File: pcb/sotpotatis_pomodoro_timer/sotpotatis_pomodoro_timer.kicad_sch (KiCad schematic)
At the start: 46 parts, among them J2 USB_C_PWR_IN, SW1 LEFT_BTN, SW2 PRESET_1_BTN, SW3 PRESET_2_BTN, SW4 PRESET_3_BTN, SW5 RIGHT_BTN, SW6 PWR_SWITCH, U1 ATtiny84A-P

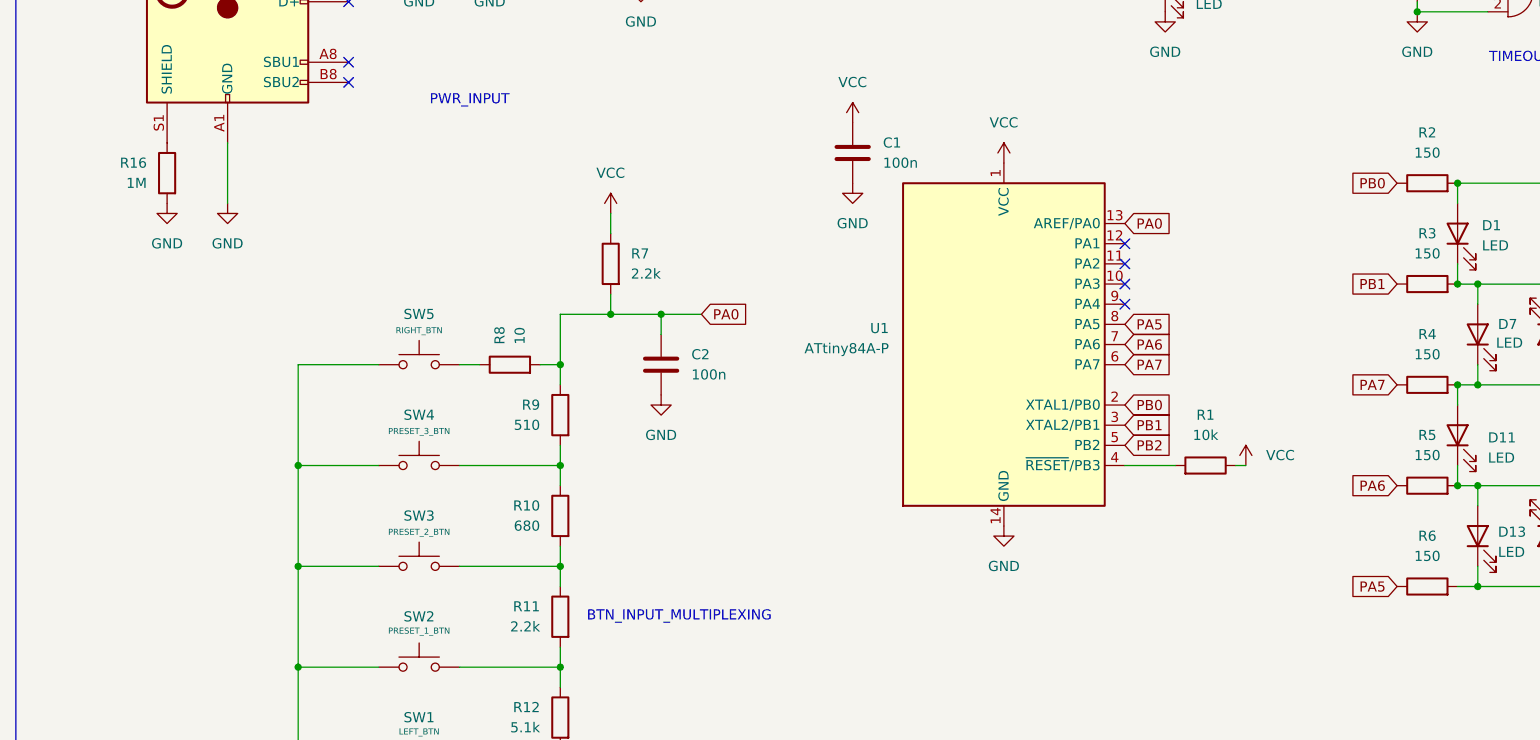
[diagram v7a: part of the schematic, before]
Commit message: fix: Remove 1M shield resistor, component relabels for better layout
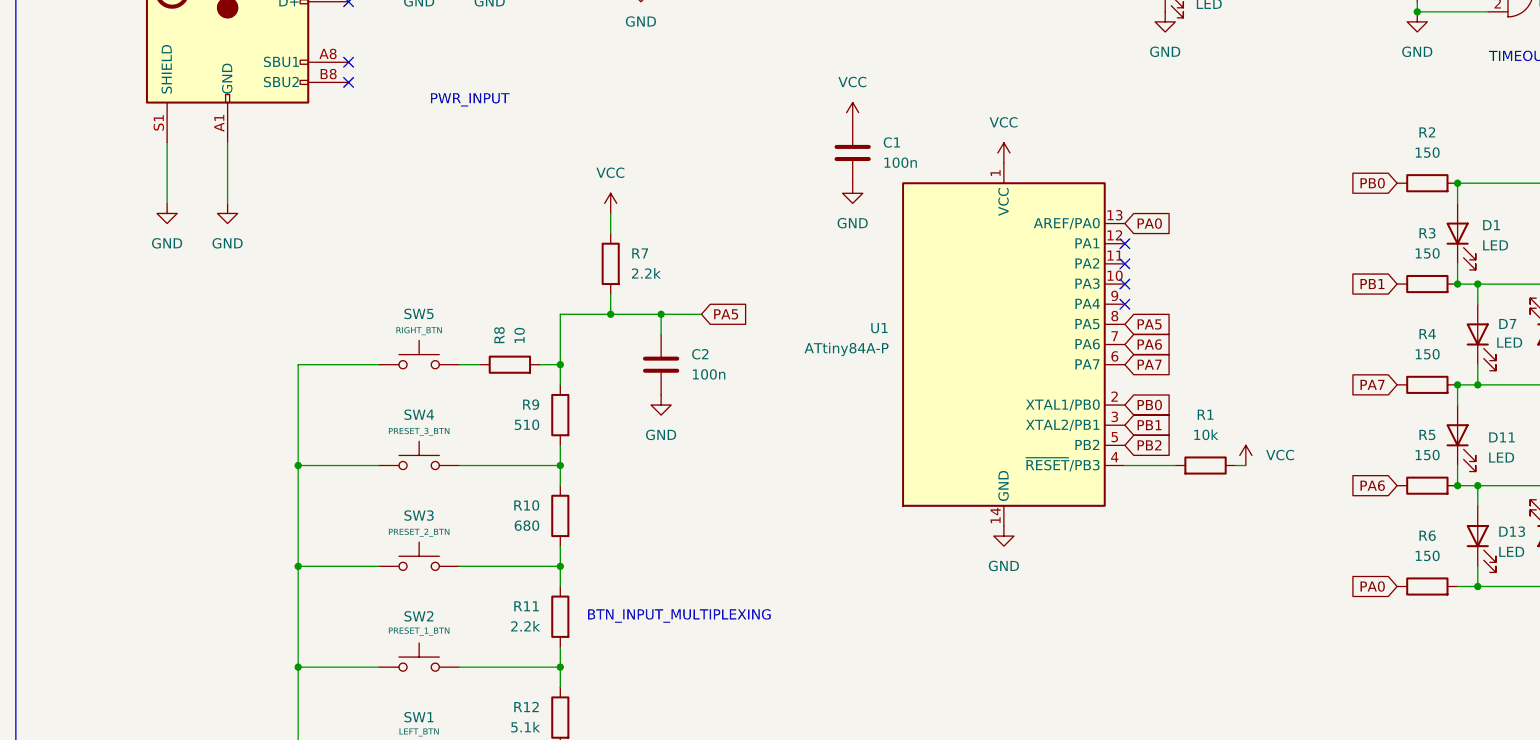
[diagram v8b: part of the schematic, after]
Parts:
- removed R16: 1M, Resistor_SMD:R_0805_2012Metric_Pad1.20x1.40mm_HandSolder, symbol Device:R
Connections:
- net GND: now also J2.S1 (SHIELD)
- net PA0: now also R6.1; no longer C2.1, R7.2, R8.2, R9.1
- net PA5: now also C2.1, R7.2, R8.2, R9.1; no longer R6.1
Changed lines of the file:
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@@
+	(wire
+		(pts
+			(xy 31.75 83.82) (xy 31.75 91.44)
+		)
+		(stroke
+			(width 0)
+			(type default)
+		)
+	)
 	(wire
 		(pts
@@
 		)
 	)
-	(global_label "PA5"
+	(global_label "PA0"
 		(shape input)
 		(at 186.69 139.7 180)
@@
 		)
 	)
-	(global_label "PA0"
+	(global_label "PA5"
 		(shape input)
 		(at 99.06 105.41 0)
@@
 					(unit 1)
 				)
-			)
-		)
-	)
-	(symbol
-		(lib_id "Device:R")
-		(at 31.75 87.63 0)
-		(mirror y)
-		(unit 1)
-		(exclude_from_sim no)
-		(in_bom yes)
-		(on_board yes)
-		(dnp no)
-		(property "Reference" "R16"
-			(at 29.21 86.3599 0)
-			(effects
-				(font
-					(size 1.27 1.27)
-				)
-				(justify left)
-			)
-		)
-		(property "Value" "1M"
-			(at 29.21 88.8999 0)
-			(effects
-				(font
-					(size 1.27 1.27)
-				)
-				(justify left)
-			)
-		)
-		(property "Footprint" "Resistor_SMD:R_0805_2012Metric_Pad1.20x1.40mm_HandSolder"
-			(at 33.528 87.63 90)
-			(effects
-				(font
-					(size 1.27 1.27)
-				)
-				(hide yes)
-			)
-		)
-		(property "Datasheet" "~"
-			(at 31.75 87.63 0)
-			(effects
-				(font
-					(size 1.27 1.27)
-				)
-				(hide yes)
-			)
-		)
-		(property "Description" "Resistor"
-			(at 31.75 87.63 0)
-			(effects
-				(font
-					(size 1.27 1.27)
-				)
-				(hide yes)
-			)
-		)
-		(pin "1"
-		)
-		(pin "2"
-		)
-		(instances
-			(project ""
-				(path "/fd9fadc6-6513-48e8-84bb-1df0990bb3d5"
-					(reference "R16")
-					(unit 1)
-				)
